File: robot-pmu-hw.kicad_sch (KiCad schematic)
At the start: 4 parts

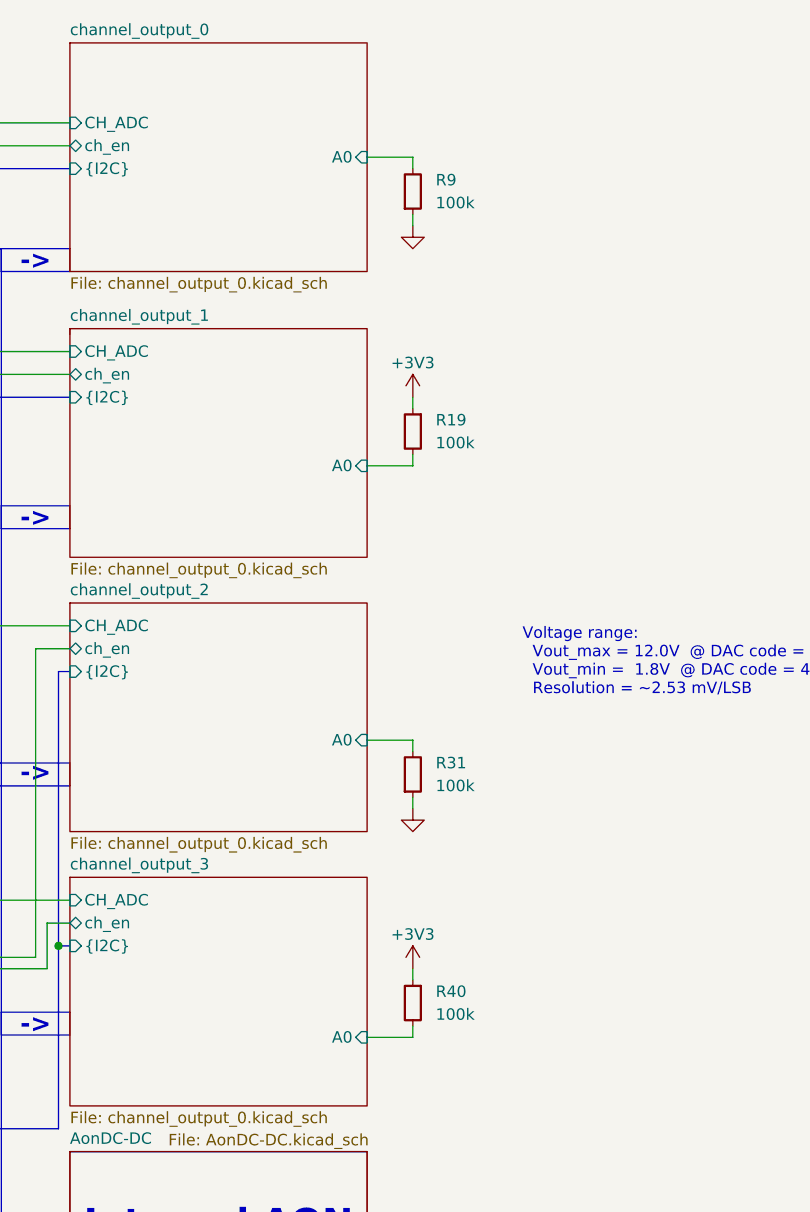
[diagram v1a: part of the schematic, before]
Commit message: Remove redundant resistors
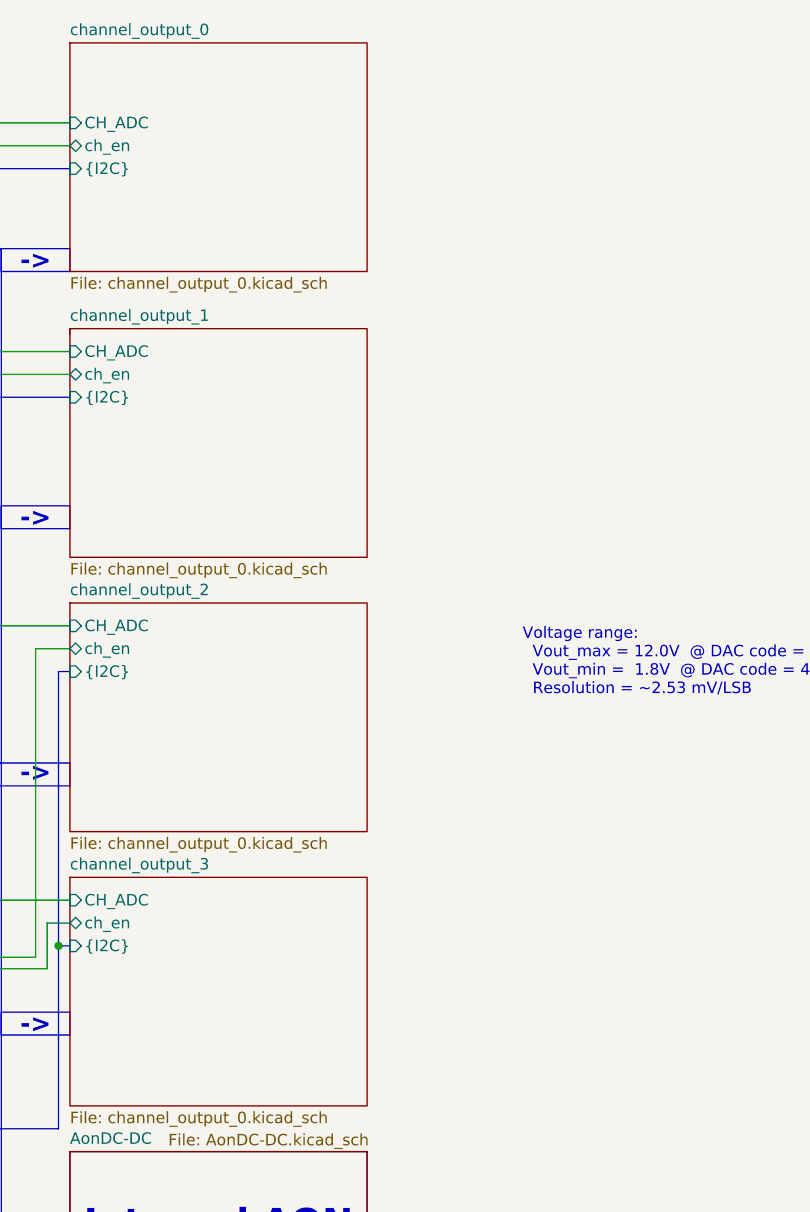
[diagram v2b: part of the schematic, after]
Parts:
- removed R19, R31, R40, R9: R_100k_0402, Hardware Components Footprints:R_0402_1005Metric, symbol Hardware Components:R_100k_0402
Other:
- sheet channel_output_0 ports: added none; removed A0
- sheet channel_output_1 ports: added none; removed A0
- sheet channel_output_2 ports: added none; removed A0
- sheet channel_output_3 ports: added none; removed A0

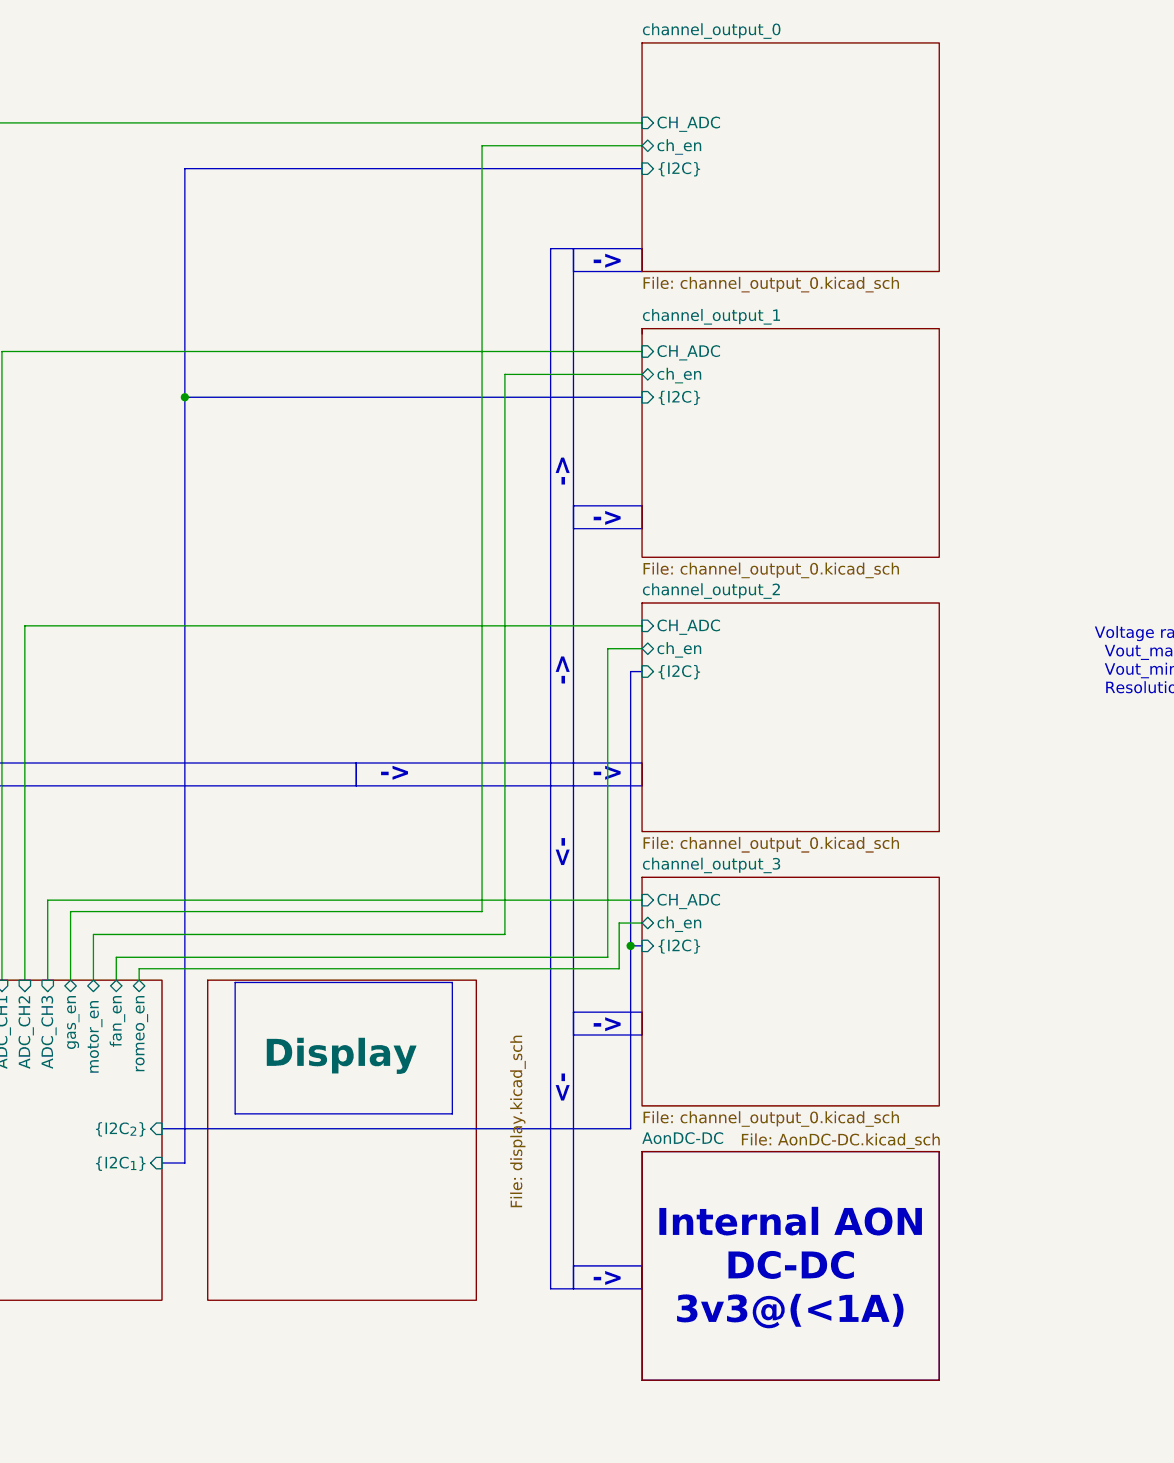
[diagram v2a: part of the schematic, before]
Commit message: Add lead compensator, move leds to uC, redo resistors
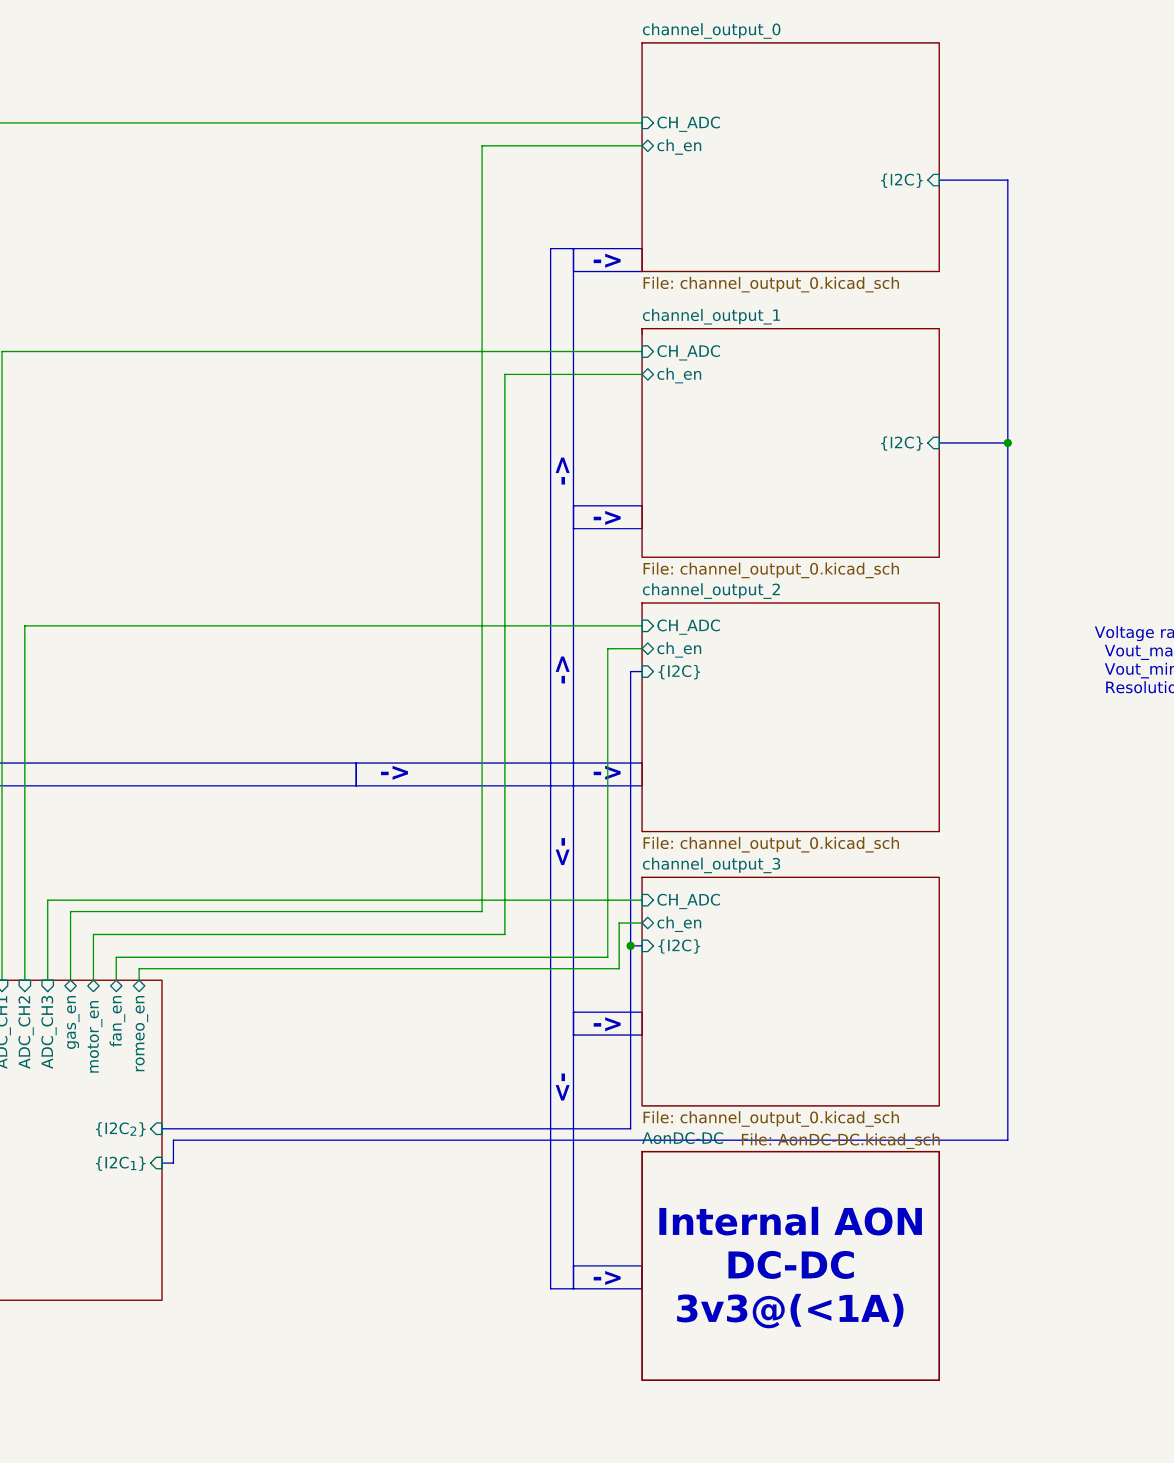
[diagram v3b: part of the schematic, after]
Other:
- removed sheet Display
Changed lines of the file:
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@@
-		)
-	)
-	(text_box " \n"
-		(exclude_from_sim no)
-		(at 222.758 160.274 0)
-		(size 24.13 14.605)
-		(margins 0.9525 0.9525 0.9525 0.9525)
-		(stroke
-			(width 0)
-			(type solid)
-			(color 108 142 191 1)
-		)
-		(fill
-			(type color)
-			(color 218 232 252 1)
-		)
-		(effects
-			(font
-				(size 2.5 2.5)
-				(thickness 0.3125)
-				(color 0 0 0 1)
-			)
 		)
 	)
@@
 	)
 	(junction
-		(at 217.17 95.25)
+		(at 308.61 100.33)
 		(diameter 0)
 		(color 0 0 0 0)
@@
 	(bus
 		(pts
-			(xy 217.17 95.25) (xy 217.17 180.34)
+			(xy 308.61 71.12) (xy 308.61 100.33)
 		)
 		(stroke
@@
 			(width 0)
 			(type default)
+			(color 194 194 0 1)
 		)
 	)
@@
 			(width 0)
 			(type default)
+			(color 194 194 0 1)
 		)
 	)
@@
 		)
 	)
+	(bus
+		(pts
+			(xy 300.99 100.33) (xy 308.61 100.33)
+		)
+		(stroke
+			(width 0)
+			(type default)
+		)
+	)
 	(wire
 		(pts
@@
 			(width 0)
 			(type default)
+			(color 194 194 0 1)
 		)
 	)
@@
 			(width 0)
 			(type default)
+			(color 194 194 0 1)
 		)
 	)
@@
 			(width 0)
 			(type default)
+			(color 194 194 0 1)
 		)
 	)
@@
 			(width 0)
 			(type default)
+			(color 194 194 0 1)
 		)
 	)
@@
 			(width 0)
 			(type default)
+			(color 194 194 0 1)
 		)
 	)
@@
 	(bus
 		(pts
-			(xy 267.97 69.85) (xy 217.17 69.85)
+			(xy 300.99 71.12) (xy 308.61 71.12)
 		)
 		(stroke
@@
 			(width 0)
 			(type default)
+			(color 194 194 0 1)
 		)
 	)
@@
 			(width 0)
 			(type default)
+			(color 194 194 0 1)
 		)
 	)
@@
 			(width 0)
 			(type default)
+			(color 194 194 0 1)
+		)
+	)
+	(bus
+		(pts
+			(xy 215.9 180.34) (xy 215.9 177.8)
+		)
+		(stroke
+			(width 0)
+			(type default)
 		)
 	)
@@
 			(width 0)
 			(type default)
+			(color 194 194 0 1)
 		)
 	)
@@
 			(width 0)
 			(type default)
+			(color 194 194 0 1)
 		)
 	)
@@
 			(width 0)
 			(type default)
+			(color 194 194 0 1)
 		)
 	)
@@
 	(bus
 		(pts
-			(xy 217.17 180.34) (xy 214.63 180.34)
+			(xy 308.61 177.8) (xy 215.9 177.8)
 		)
 		(stroke
@@
 			(width 0)
 			(type default)
+			(color 194 194 0 1)
 		)
 	)
@@
 			(width 0)
 			(type default)
-		)
-	)
-	(bus
-		(pts
-			(xy 217.17 69.85) (xy 217.17 95.25)
+			(color 194 194 0 1)
+		)
+	)
+	(bus
+		(pts
+			(xy 214.63 180.34) (xy 215.9 180.34)
 		)
 		(stroke
@@
 			(width 0)
 			(type default)
+			(color 194 194 0 1)
+		)
+	)
+	(bus
+		(pts
+			(xy 308.61 100.33) (xy 308.61 177.8)
+		)
+		(stroke
+			(width 0)
+			(type default)
 		)
 	)
@@
 			(width 0)
 			(type default)
-		)
-	)
-	(bus
-		(pts
-			(xy 267.97 95.25) (xy 217.17 95.25)
-		)
-		(stroke
-			(width 0)
-			(type default)
+			(color 194 194 0 1)
 		)
 	)
@@
 		)
 		(pin "{I2C}" input
-			(at 267.97 95.25 180)
-			(effects
-				(font
-					(size 1.27 1.27)
-				)
-				(justify left)
+			(at 300.99 100.33 0)
+			(effects
+				(font
+					(size 1.27 1.27)
+				)
+				(justify right)
 			)
 		)
@@
 		)
 		(pin "{I2C}" input
-			(at 267.97 69.85 180)
-			(effects
-				(font
-					(size 1.27 1.27)
-				)
-				(justify left)
+			(at 300.99 71.12 0)
+			(effects
+				(font
+					(size 1.27 1.27)
+				)
+				(justify right)
 			)
 		)
@@
 				)
 			)
-		)
-	)
-	(sheet
-		(at 219.71 160.02)
-		(size 29.845 35.56)
-		(exclude_from_sim no)
-		(in_bom yes)
-		(on_board yes)
-		(dnp no)
-		(stroke
-			(width 0.1524)
-			(type solid)
-		)
-		(fill
-			(color 108 142 191 1.0000)
-		)
-		(property "Sheetname" "Display"
-			(at 234.442 168.148 0)
-			(effects
-				(font
-					(size 3 3)
-					(thickness 0.254)
-					(bold yes)
-					(color 0 0 0 1)
-				)
-			)
-		)
-		(property "Sheetfile" "display.kicad_sch"
-			(at 253.3146 185.42 90)
-			(effects
-				(font
-					(size 1.27 1.27)
-				)
-				(justify left top)
-			)
-		)
-		(instances
-			(project "robot-pmu-hw"
-				(path "/ca7f4c4c-3c96-472a-b66f-ec124f8cf9b5"
-					(page "9")
-				)
-			)
